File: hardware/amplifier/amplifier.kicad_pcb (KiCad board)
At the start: 2 copper layers, 50 x 50 mm, 6 parts, among them M1 MountingHole_3.2mm_M3_Pad, M2 MountingHole_3.2mm_M3_Pad, M3 MountingHole_3.2mm_M3_Pad, M4 MountingHole_3.2mm_M3_Pad, P2 OUT, X1 IN

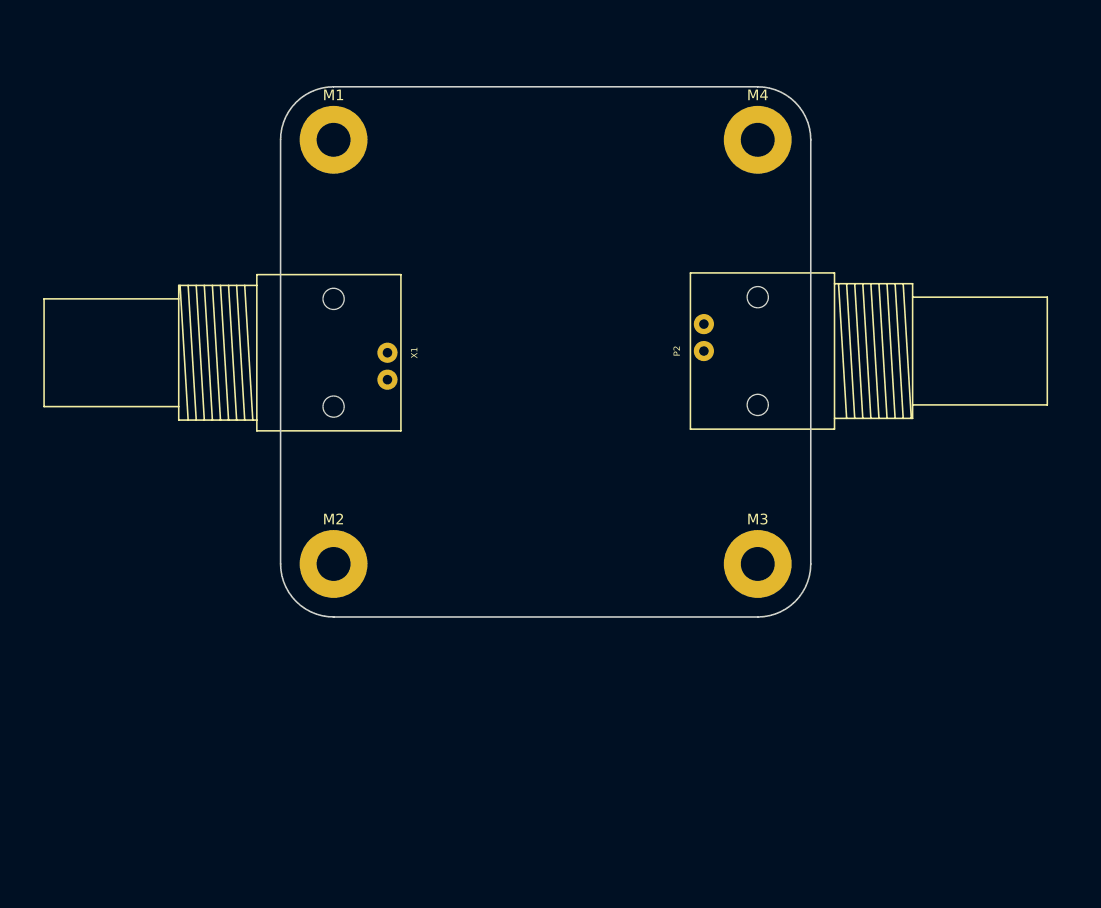
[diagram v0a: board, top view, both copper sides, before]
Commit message: schema done for now; needs some minor changes; routing done for this schema
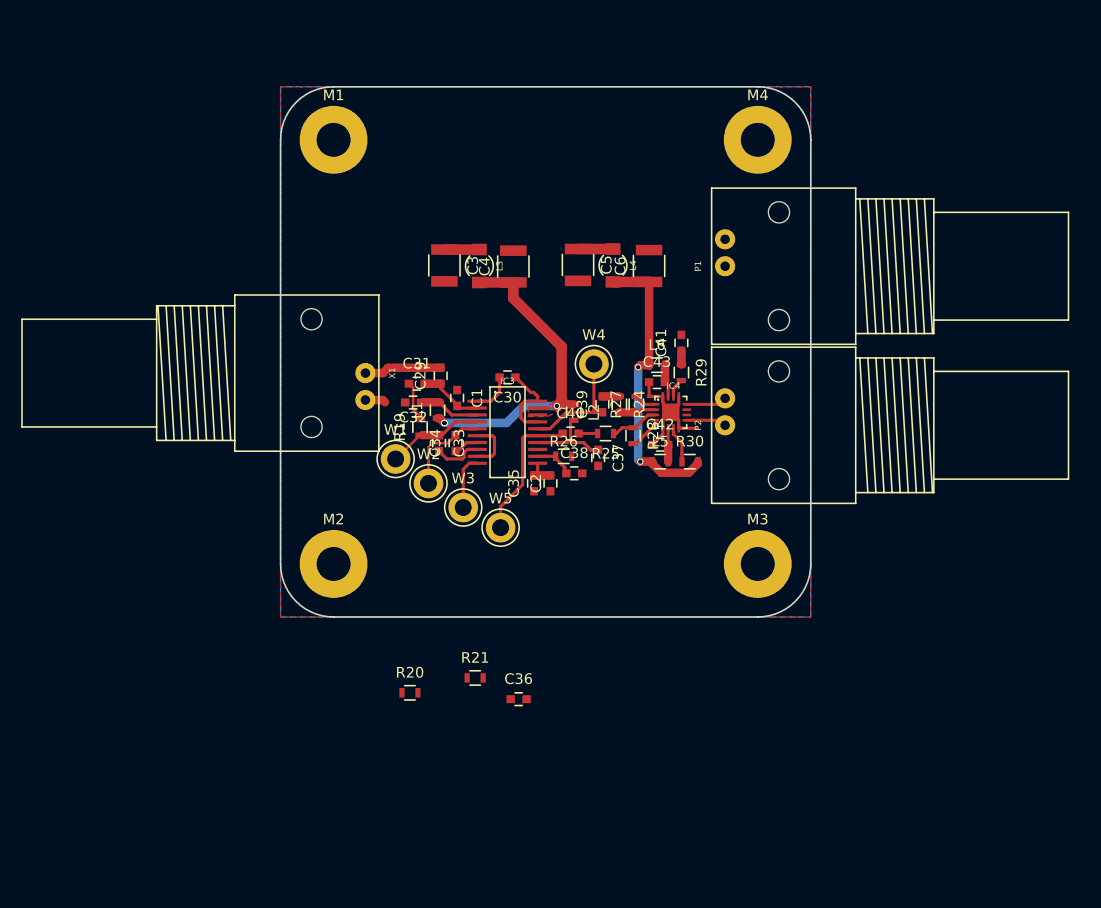
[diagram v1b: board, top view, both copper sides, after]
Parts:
- added C1: 22p, Capacitors_SMD:C_0603, F.Cu at (116.7, 79.3)
- added C2: 1n, Capacitors_SMD:C_0603, F.Cu at (125.5, 87.4)
- added C29: 100n, Capacitors_SMD:C_0603, F.Cu at (115.1, 77.2)
- added C3: 22u, Capacitors_SMD:C_1210, F.Cu at (115.5, 66.8)
- added C30: 100n, Capacitors_SMD:C_0603, F.Cu at (121.4, 77.4)
- added C31: 18n, Capacitors_SMD:C_0603, F.Cu at (112.8, 78.0)
- added C32: 100n, Capacitors_SMD:C_0603, F.Cu at (112.5, 79.8)
- added C33: 100n, Capacitors_SMD:C_0603, F.Cu at (115.0, 83.6)
- added C34: 100n, Capacitors_SMD:C_0603, F.Cu at (116.5, 83.6)
- added C35: 100n, Capacitors_SMD:C_0603, F.Cu at (123.9, 87.4)
- added C36: 1u, Capacitors_SMD:C_0603, F.Cu at (122.5, 107.8)
- added C37: 100n, Capacitors_SMD:C_0603, F.Cu at (129.9, 85.0)
- added C38: 100n, Capacitors_SMD:C_0603, F.Cu at (127.7, 86.5)
- added C39: 100n, Capacitors_SMD:C_0603, F.Cu at (130.3, 80.0)
- added C4: 22u, Capacitors_SMD:C_1210, F.Cu at (122.0, 67.0)
- added C40: 100n, Capacitors_SMD:C_0603, F.Cu at (127.3, 82.7)
- added C41: 100n, Capacitors_SMD:C_0603, F.Cu at (137.8, 74.2)
- added C42: 100n, Capacitors_SMD:C_0603, F.Cu at (135.8, 83.8)
- added C43: 100n, Capacitors_SMD:C_0603, F.Cu at (135.5, 77.8)
- added C5: 22u, Capacitors_SMD:C_1210, F.Cu at (128.1, 66.8)
- added C6: 22u, Capacitors_SMD:C_1210, F.Cu at (134.8, 66.9)
- added IC3: AD8331, SDRfootprints:QSOP20, F.Cu at (118.5, 79.7)
- added IC4: ISL55210, SDRfootprints:TQFN16, F.Cu at (135.3, 80.0)
- added L1: 120n, Resistors_SMD:R_0603, F.Cu at (114.8, 80.5)
- added L2: 120n, Resistors_SMD:R_0603, F.Cu at (127.7, 80.7)
- added L3: 22u, SDRfootprints:COIL_445-4177-1-ND, F.Cu at (118.8, 65.3)
- added L4: 22u, SDRfootprints:COIL_445-4177-1-ND, F.Cu at (131.3, 65.3)
- added L5: 120n, Resistors_SMD:R_0603, F.Cu at (135.8, 85.3)
- added L6: 120n, Resistors_SMD:R_0603, F.Cu at (135.5, 76.2)
- added P1: OUT, SDRfootprints:1-1337543-0, F.Cu at (141.9, 64.4)
- added R19: 274R, Resistors_SMD:R_0603, F.Cu at (113.2, 82.1)
- added R20: 8k2, Resistors_SMD:R_0603, F.Cu at (112.2, 107.2)
- added R21: 3k9, Resistors_SMD:R_0603, F.Cu at (118.3, 105.8)
- added R24: 270R, Resistors_SMD:R_0603, F.Cu at (131.9, 80.0)
- added R25: 270R, Resistors_SMD:R_0603, F.Cu at (130.7, 82.7)
- added R26: 3k9, Resistors_SMD:R_0603, F.Cu at (126.7, 84.8)
- added R27: 8k2, Resistors_SMD:R_0603, F.Cu at (133.6, 80.0)
- added R28: 8k2, Resistors_SMD:R_0603, F.Cu at (133.2, 82.9)
- added R29: 200R, Resistors_SMD:R_0603, F.Cu at (137.8, 77.0)
- added R30: 10k, Resistors_SMD:R_0603, F.Cu at (138.6, 85.3)
- added W1: TEST_1P, Measurement_Points:Test_Point_Keystone_5005-5009_Compact, F.Cu at (110.8, 85.1)
- added W2: TEST_1P, Measurement_Points:Test_Point_Keystone_5005-5009_Compact, F.Cu at (114.0, 87.4)
- added W3: TEST_1P, Measurement_Points:Test_Point_Keystone_5005-5009_Compact, F.Cu at (117.2, 89.7)
- added W4: TEST_1P, Measurement_Points:Test_Point_Keystone_5005-5009_Compact, F.Cu at (129.6, 76.2)
- added W5: TEST_1P, Measurement_Points:Test_Point_Keystone_5005-5009_Compact, F.Cu at (120.8, 91.6)
- moved P2 7.28 mm to (141.9, 79.4)
- moved X1 2.83 mm to (108.0, 79.5)
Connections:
- X1 pad 2: Net-(X1-Pad2) -> GNDA
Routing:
- net +5VA: track 0.00 -> 32.7 mm, vias 0 -> 3
- net GNDA: track 0.00 -> 28.5 mm
- net +3.3VADC: track 0.00 -> 27.9 mm, vias 0 -> 2
- net Net-(C40-Pad1): track 0.00 -> 13.3 mm
- net Net-(C39-Pad1): track 0.00 -> 11.3 mm
- net Net-(C33-Pad1): track 0.00 -> 9.15 mm
- net Net-(C34-Pad2): track 0.00 -> 8.89 mm
- net Net-(C37-Pad1): track 0.00 -> 7.94 mm
- net Net-(C29-Pad2): track 0.00 -> 7.31 mm
- net Net-(C1-Pad2): track 0.00 -> 6.22 mm
- net Net-(C32-Pad1): track 0.00 -> 5.75 mm
- net Net-(C36-Pad2): track 0.00 -> 5.16 mm
- net Net-(IC4-Pad3): track 0.00 -> 4.62 mm
- net Net-(C33-Pad2): track 0.00 -> 4.56 mm
- net Net-(C31-Pad1): track 0.00 -> 3.88 mm
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- added copper zone on F.Cu, net +5VA
- added copper zone on B.Cu, net GNDA
- added copper zone on F.Cu, net GNDA

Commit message: amp done
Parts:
- removed M1, M2, M3, M4: MountingHole_3.2mm_M3_Pad, Mounting_Holes:MountingHole_3.2mm_M3_Pad
- removed R20: 8k2, Resistors_SMD:R_0603
- removed R21: 3k9, Resistors_SMD:R_0603
- added C11: 100n, Capacitors_SMD:C_0603, F.Cu at (112.7, 92.8)
- added C4: 100n, Capacitors_SMD:C_0603, F.Cu at (119.5, 95.0)
- added R1: 330k, Resistors_SMD:R_0603, F.Cu at (115.3, 97.0)
- added R2: 82k, Resistors_SMD:R_0603, F.Cu at (119.5, 97.0)
- added U1: MCP4706/16/26, TO_SOT_Packages_SMD:SOT-23-6, F.Cu at (116.2, 94.0)
- X2: renamed from P1; value OUT -> OUT_1
- X3: renamed from P2; value OUT -> OUT_2
- moved C12 21.4 mm to (117.9, 86.8), turned to 180 degrees
- moved W4 4.43 mm to (129.4, 71.7)
- moved W1 1.50 mm to (109.3, 85.0)
- moved W2 1.38 mm to (112.6, 87.1)
- renumbered C29 to C1, C35 to C10, C36 to C12, C3 to C13, C37 to C14, C4 to C15, C38 to C16, C5 to C17, C39 to C18, C40 to C19, C1 to C2, C6 to C20, C41 to C21, C42 to C22, C43 to C23, C30 to C3, C31 to C5, C32 to C6, C33 to C7, C34 to C8, C2 to C9, IC3 to IC1, IC4 to IC2, R30 to R10, R19 to R3, R26 to R4, R24 to R5, R25 to R6, R27 to R7, R28 to R8, R29 to R9
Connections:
- C12 pad 1: GND -> GNDA
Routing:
- net GNDA: track 28.5 -> 189.0 mm, vias 0 -> 123
- net Net-(C19-Pad2): track 1.80 -> 25.8 mm, vias 0 -> 1
- net +5VA: track 32.7 -> 52.9 mm
- net Net-(C18-Pad2): track 1.60 -> 20.1 mm, vias 0 -> 2
- net Net-(C4-Pad1): track 0.00 -> 6.25 mm
- net Net-(C18-Pad1): track 11.3 -> 16.9 mm
- net Net-(C12-Pad2): track 5.16 -> 9.38 mm
- net +3.3VADC: track 27.9 -> 29.6 mm
- net Net-(C7-Pad1): track 9.15 -> 10.6 mm
- net Net-(C8-Pad2): track 8.89 -> 9.50 mm

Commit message: Amp PCB completely done with power taps and baluns
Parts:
- added C24: TBD, Capacitors_SMD:C_0603, F.Cu at (141.4, 79.8)
- added C25: TBD, Capacitors_SMD:C_0603, F.Cu at (137.3, 74.5)
- added J1: 0, Resistors_SMD:R_0603, F.Cu at (111.4, 91.8)
- added P1: 5V, Pin_Headers:Pin_Header_Angled_1x02, F.Cu at (113.2, 54.0)
- added P2: 3V3, Pin_Headers:Pin_Header_Angled_1x02, F.Cu at (125.8, 54.0)
- added P3: Interface, Pin_Headers:Pin_Header_Angled_1x03, F.Cu at (126.2, 95.9)
- added R14: TBD, Resistors_SMD:R_0603, F.Cu at (138.5, 79.8)
- added R15: 10k, Resistors_SMD:R_0603, F.Cu at (116.8, 95.5)
- added R16: 10k, Resistors_SMD:R_0603, F.Cu at (118.4, 98.0)
- added R5: TBD, Resistors_SMD:R_0603, F.Cu at (129.7, 86.7)
- added R6: TBD, Resistors_SMD:R_0603, F.Cu at (128.4, 89.4)
- added R9: 10k, Resistors_SMD:R_0603, F.Cu at (135.1, 84.8)
- added T1: BALUN, SDRfootprints:CX2041NLT, F.Cu at (139.4, 71.0)
- added T2: BALUN, SDRfootprints:CX2041NLT, F.Cu at (132.0, 90.0)
- R12: renamed from R9; value 200R -> 200
- R13: renamed from R10; value 10k -> TBD
- R3: value 274R -> 274
- R7: renamed from R5; value 270R -> 270
- R8: renamed from R6; value 270R -> 270
- moved X3 14.0 mm to (138.5, 93.0), turned to 180 degrees
- moved X1 8.00 mm to (108.0, 71.5)
- moved C11 5.96 mm to (106.8, 94.1)
- moved C4 5.96 mm to (113.7, 96.3)
- moved R2 5.96 mm to (113.7, 98.3)
- moved U1 5.96 mm to (110.4, 95.2)
- moved R1 5.96 mm to (109.5, 98.3)
- moved C14 4.13 mm to (125.8, 85.0)
- moved R13 3.85 mm to (138.5, 81.5)
- moved C16 3.80 mm to (124.0, 87.4), turned to 270 degrees
- moved X2 3.31 mm to (142.9, 67.5)
- moved C17 3.00 mm to (125.0, 66.8)
- moved W4 3.00 mm to (126.4, 71.7)
- moved C1 3.00 mm to (112.1, 77.2)
- moved C10 3.00 mm to (120.9, 87.4)
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- renumbered R7 to R10, R8 to R11
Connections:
- R13 pad 1: Net-(IC2-Pad7) -> Net-(IC2-Pad9)
- R13 pad 2: +3.3VADC -> /OUT1-
- U1 pad 1: Net-(C12-Pad2) -> Net-(J1-Pad2)
- X2 pad 1: Net-(C18-Pad2) -> Net-(T1-Pad1)
- X2 pad 2: Net-(C19-Pad2) -> GNDA
- X3 pad 1: Net-(IC2-Pad9) -> Net-(T2-Pad1)
- X3 pad 2: Net-(IC2-Pad12) -> GNDA
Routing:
- net GNDA: track 189.0 -> 272.7 mm, vias 123 -> 182
- net Net-(C19-Pad2): track 25.8 -> 8.61 mm, vias 1 -> 0
- net /SCL: track 0.00 -> 17.1 mm
- net /HILO: track 0.00 -> 16.6 mm
- net +5VA: track 52.9 -> 69.0 mm
- net /SDA: track 0.00 -> 13.1 mm
- net +5V: track 3.30 -> 14.6 mm
- net +3V3: track 3.30 -> 14.6 mm
- net Net-(C18-Pad2): track 20.1 -> 9.74 mm, vias 2 -> 0
- net /OUT1-: track 0.00 -> 10.1 mm
- net Net-(T2-Pad1): track 0.00 -> 8.39 mm
- net Net-(T1-Pad1): track 0.00 -> 7.79 mm
- net /OUT1+: track 0.00 -> 7.75 mm
- net /OUT2+: track 0.00 -> 2.58 mm
- net Net-(C1-Pad2): track 7.31 -> 9.78 mm
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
